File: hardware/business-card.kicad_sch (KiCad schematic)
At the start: 91 parts, among them J1 Connector, USB-TYPE-C-16P, U1 MAX7219EWG+T, U2 AMS1117, U3 ESP32-C3FH4, X1 40MHz, 15pF

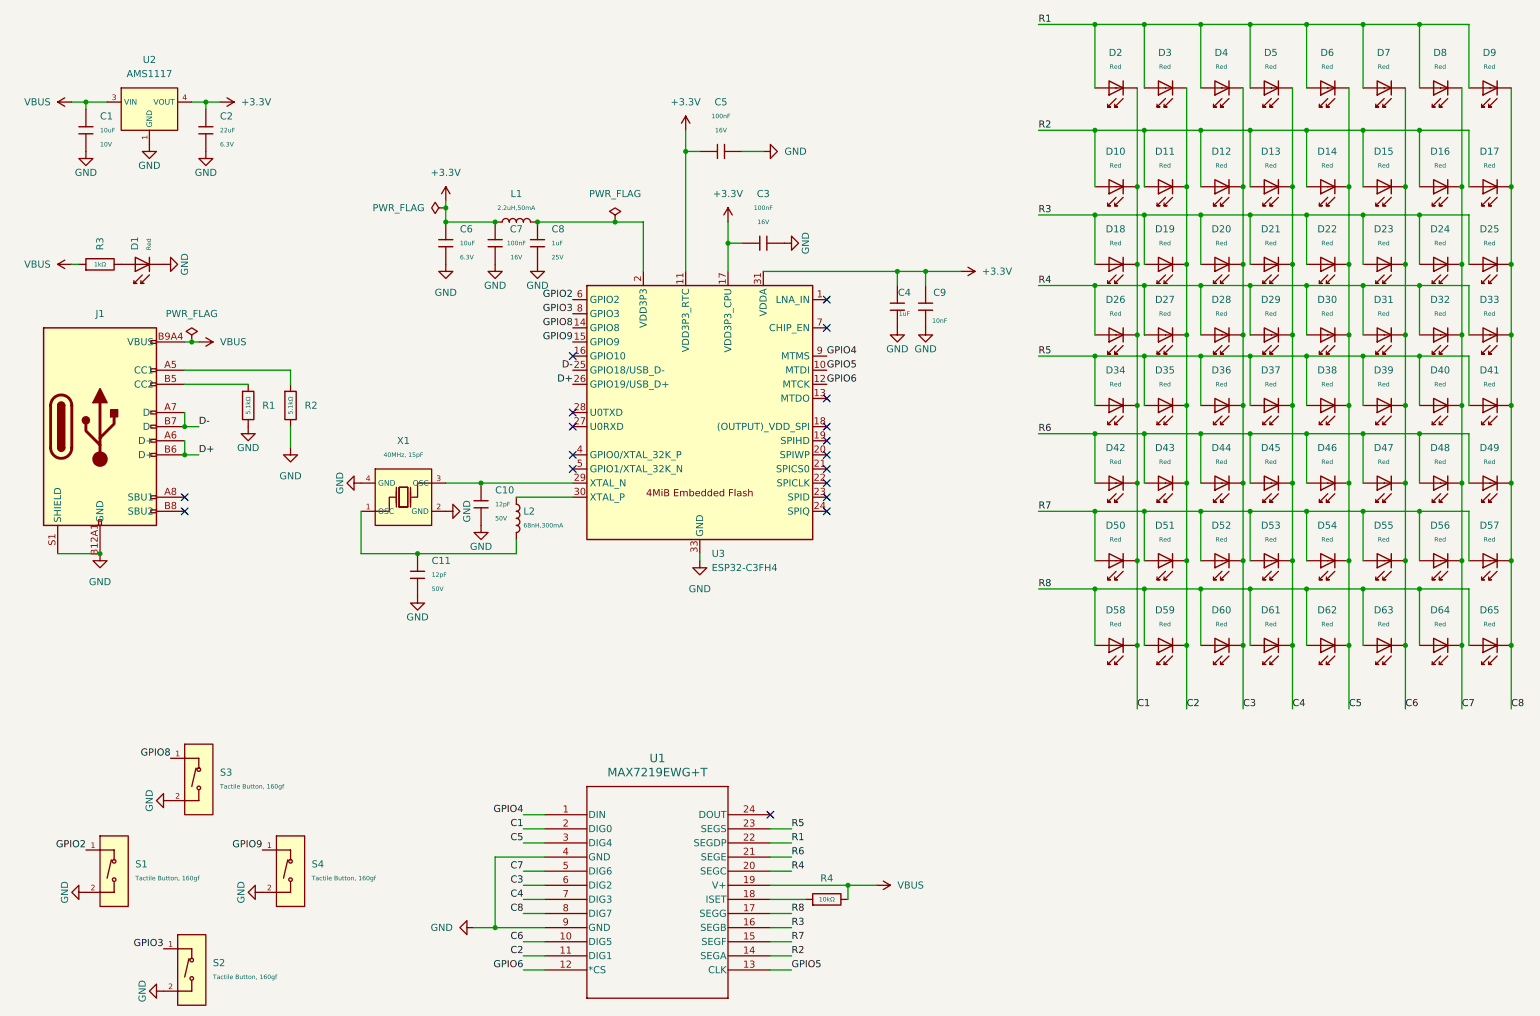
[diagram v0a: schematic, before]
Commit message: Add Kicad project to hardware
Updated the hardware directory to hold the entire kicad project. Now the
pcb can be developed on multiple kicad instances and maintained in git.
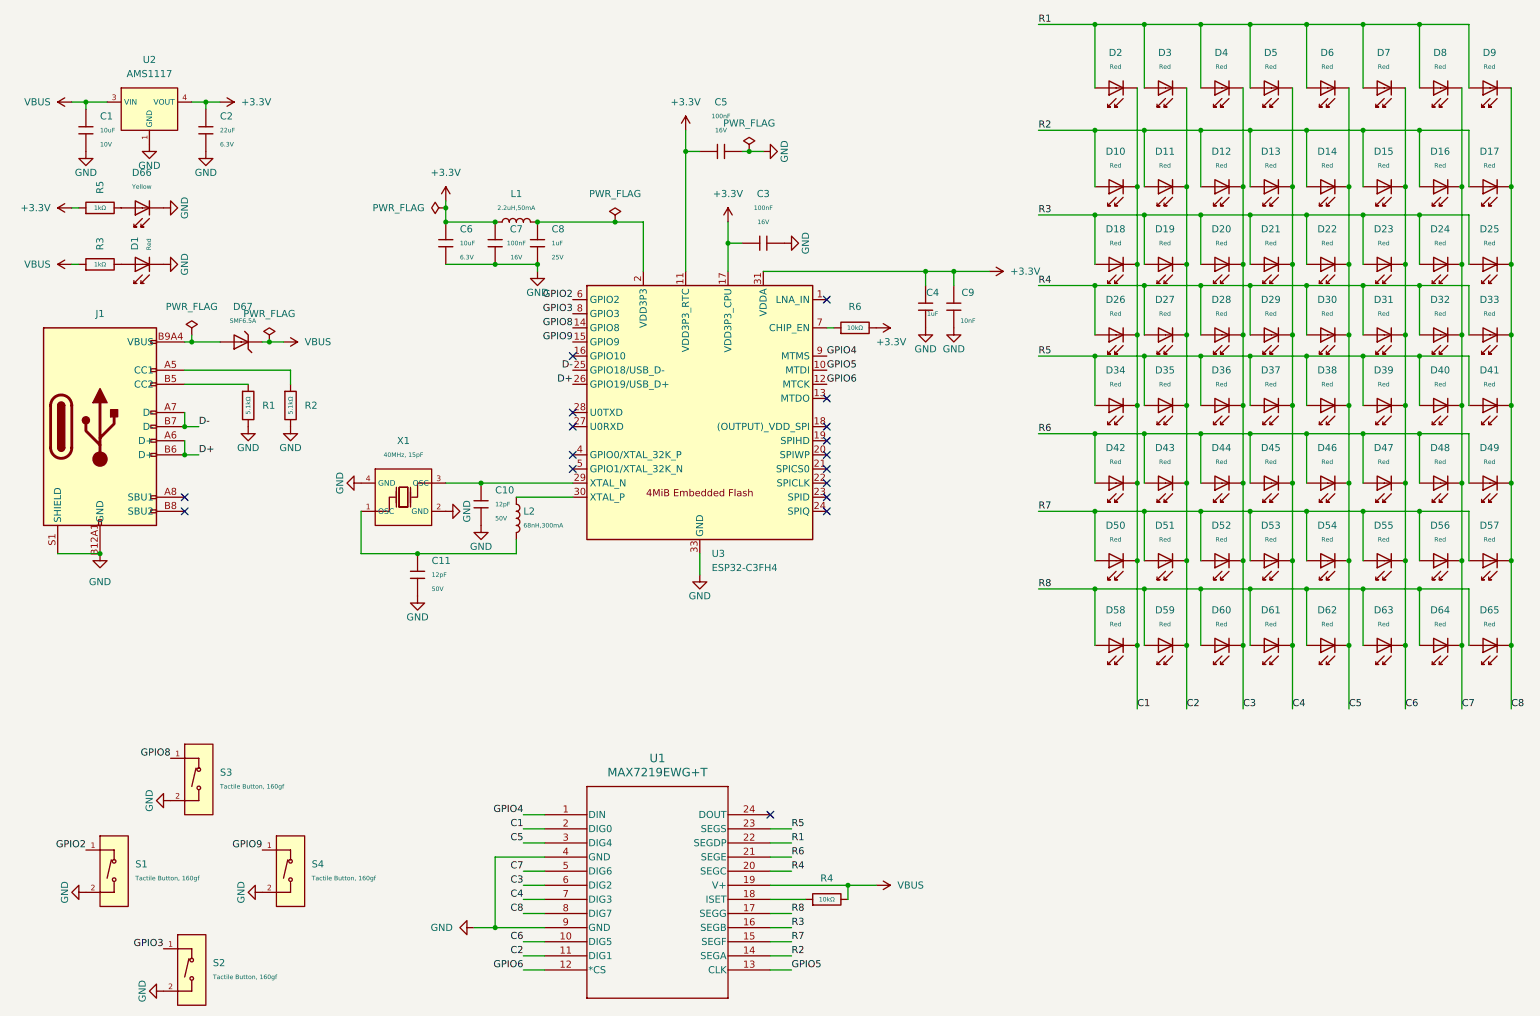
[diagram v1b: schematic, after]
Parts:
- added D66: Yellow, PCM_JLCPCB:D_0603, symbol PCM_JLCPCB-Diodes:LED,0603,Yellow
- added D67: SMF6.5A, PCM_JLCPCB:D_SOD-123FL, symbol PCM_JLCPCB-Diodes:TVS-Uni,SMF6.5A
- added R5: 1kΩ, PCM_JLCPCB:R_0402, symbol PCM_JLCPCB-Resistors:0402,1kΩ
- added R6: 10kΩ, PCM_JLCPCB:R_0402, symbol PCM_JLCPCB-Resistors:0402,10kΩ
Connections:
- net +3.3V: now also R5.1, R6.2
- net GND: now also C5.2, C6.2, R2.2, U3.33 (GND), D66.1
- net VBUS: now also D67.1; no longer J1.A9B4 (VBUS), J1.B9A4 (VBUS)
- net at U3.7 (CHIP_EN): now also R6.1
- new net: D67.2, J1.A9B4 (VBUS), J1.B9A4 (VBUS)
- new net: D66.2, R5.2
- no-connect marks 18 -> 17
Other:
- moved on the sheet: C4, C9
